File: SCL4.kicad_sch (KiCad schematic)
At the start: 37 parts, among them J2 spare2, J3 Siemens_A1010-A263, J5 SP2, J6 Conn_01x08, J7 5V out, U1 MC3487DX, U2 MC3487DX, U3 TRAM Size 2, U4 MC10H125 (20PLCC), U5 MC10H124 (20PLCC)

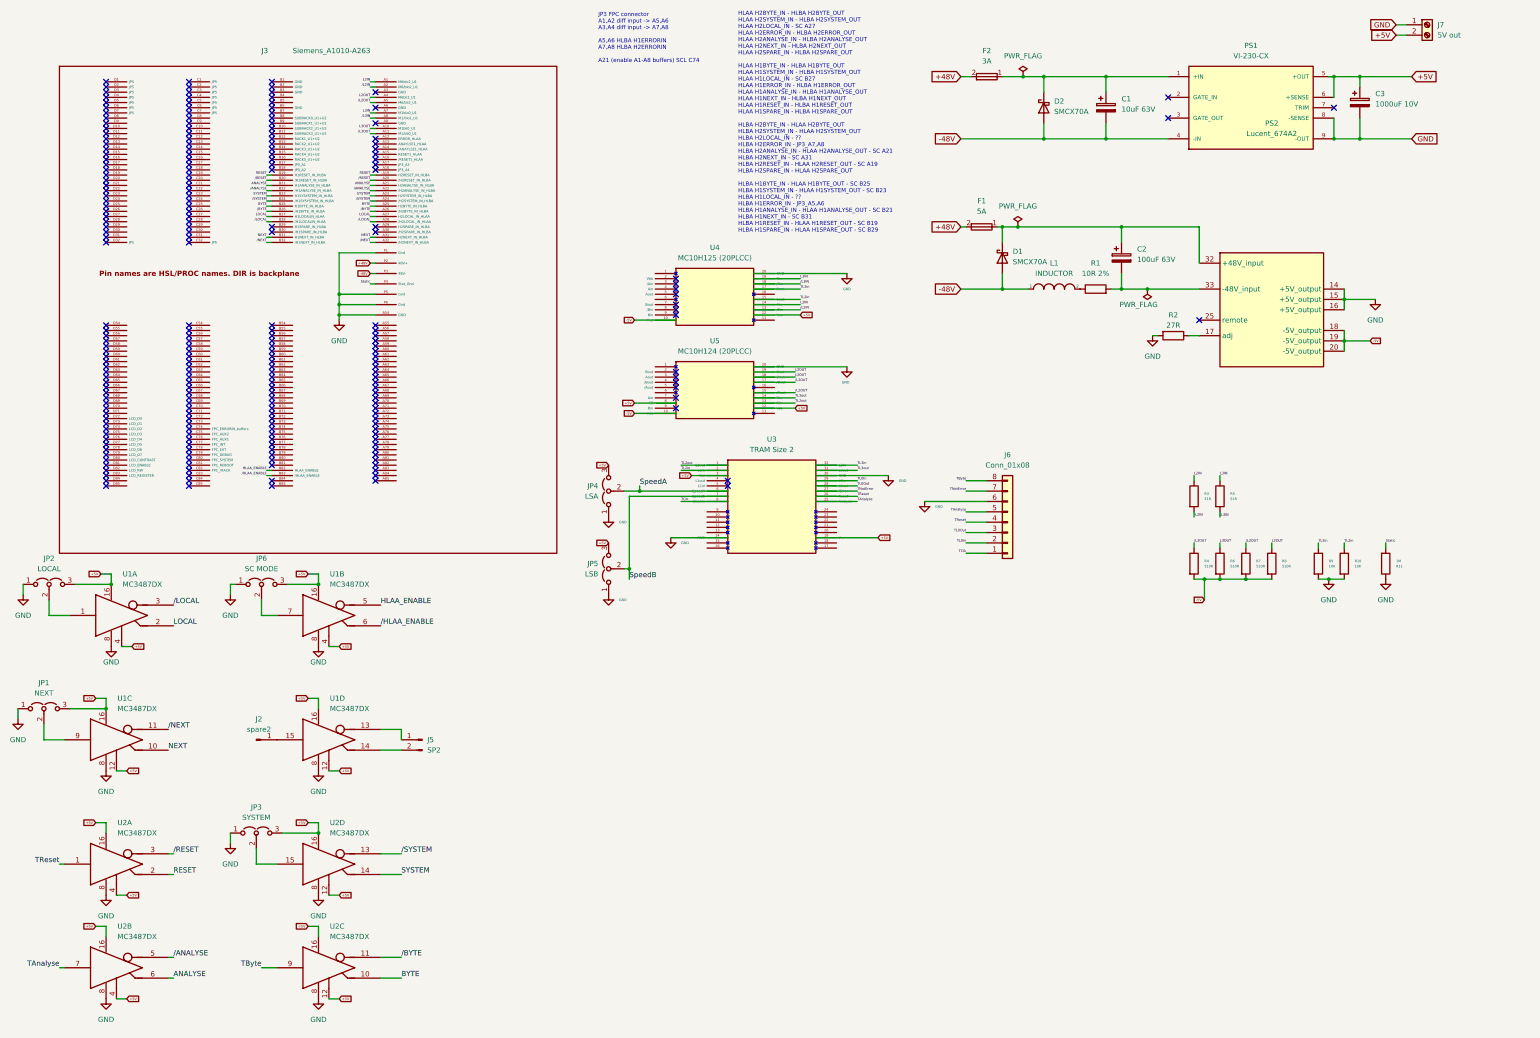
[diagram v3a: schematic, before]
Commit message: Major rework - fix -5V2 PSU orientation - analyse2 & reset2 signals for proc only operation (no HSL) - bring TRAM L1 and L3 to external header - lay down C3 to reduce height - decoupling - reduce + better match ECL trace lengths - remove R1 - reorder J6 to same as rpi interface header
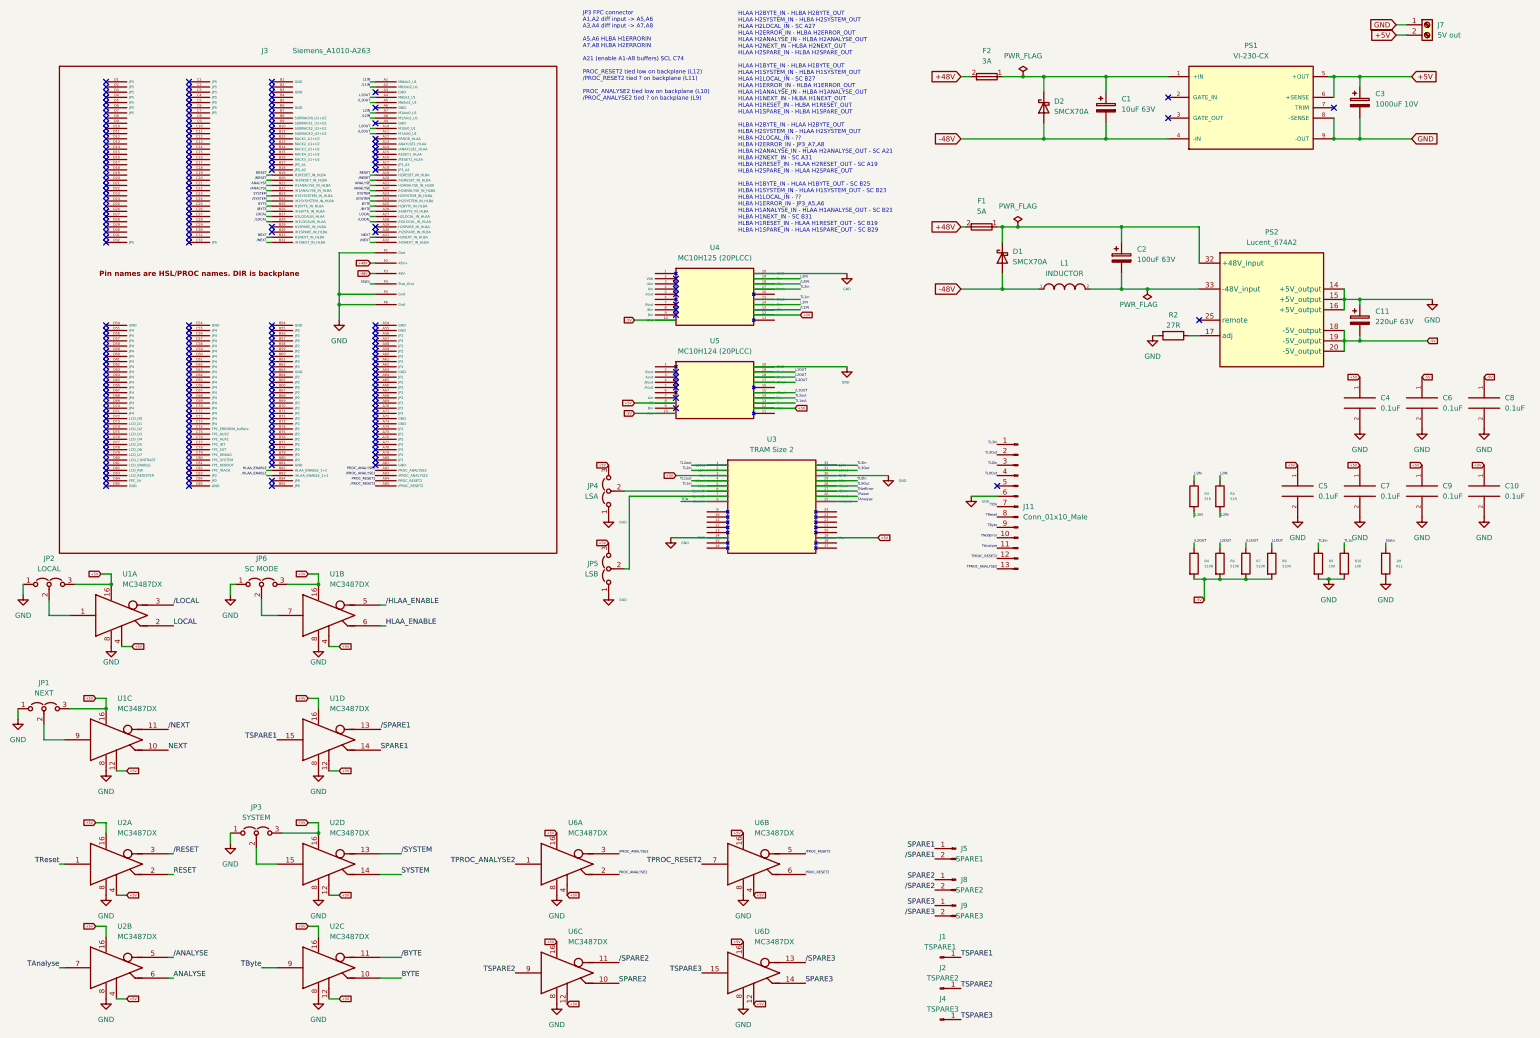
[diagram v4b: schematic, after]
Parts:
- removed J6: Conn_01x08, Connector_PinHeader_2.54mm:PinHeader_1x08_P2.54mm_Vertical, symbol Connector_Generic:Conn_01x08
- removed R1: 10R 2%, Resistor_THT:R_Axial_DIN0207_L6.3mm_D2.5mm_P15.24mm_Horizontal, symbol Device:R
- added C10, C4, C5, C6, C7, C8, C9: 0.1uF, Capacitor_SMD:C_0402_1005Metric_Pad0.74x0.62mm_HandSolder, symbol pspice:C
- added C11: 220uF 63V, Capacitor_THT:C_Radial_D8.0mm_H11.5mm_P3.50mm, symbol Device:C_Polarized
- added J1: TSPARE1, Connector_PinHeader_2.54mm:PinHeader_1x01_P2.54mm_Vertical, symbol Connector:Conn_01x01_Male
- added J11: Conn_01x10_Male, Connector_PinHeader_2.54mm:PinHeader_1x13_P2.54mm_Horizontal, symbol Connector:Conn_01x13_Male
- added J4: TSPARE3, Connector_PinHeader_2.54mm:PinHeader_1x01_P2.54mm_Vertical, symbol Connector:Conn_01x01_Male
- added J8: SPARE2, Connector_PinHeader_2.54mm:PinHeader_1x02_P2.54mm_Vertical, symbol Connector:Conn_01x02_Male
- added J9: SPARE3, Connector_PinHeader_2.54mm:PinHeader_1x02_P2.54mm_Vertical, symbol Connector:Conn_01x02_Male
- added U6: MC3487DX, Package_SO:SOIC-16_3.9x9.9mm_P1.27mm, symbol Interface_LineDriver:MC3487DX
- C3: footprint Capacitor_THT:CP_Radial_D13.0mm_P5.00mm -> Capacitor_THT:C_Radial_D12.5mm_H20.0mm_P5.00mm
- J2: value spare2 -> TSPARE2
- J5: value SP2 -> SPARE1
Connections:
- net L3IN is gone; now on net L2IN: J3.A7 (M1blo0_U1), R5.1, U4.19 (Din)
- net L3OUT is gone; now on net L2OUT: J3.A10 (M1bli0_U1), R6.1, U5.18 (Dout)
- net /L3IN is gone; now on net /L2IN: J3.A8 (M1/blo1_U1), R5.2, U4.18 (/Din)
- net /L3OUT is gone; now on net /L2OUT: J3.A11 (M1/bli0_U1), R4.1, U5.17 (/Dout)
- net +5V: now also C10.1, C4.1, C5.1, C7.1, C9.1, U6.12 (ENABLE), U6.12 (ENABLE), U6.16 (VCC), U6.16 (VCC), U6.16 (VCC), U6.16 (VCC), U6.4 (ENABLE), U6.4 (ENABLE)
- net -5V: now also C11.2, C6.1, C8.1
- net GND: now also C10.2, C11.1, C4.2, C5.2, C6.2, C7.2, C8.2, C9.2, J11.6 (Pin_6), U6.8 (GND), U6.8 (GND), U6.8 (GND), U6.8 (GND); no longer J3.A54 (GND)
- net HLAA_ENABLE: now also U1.6 (OUT+); no longer U1.5 (OUT-)
- net L2IN: no longer J3.A1 (M6blo2_U1), R3.1, U4.14 (Cin)
- net L2OUT: no longer J3.A4 (M6bli2_U1), R8.1, U5.19 (Cout)
- net TAnalyse: now also J11.11 (Pin_11)
- net TByte: now also J11.9 (Pin_9)
- net TClk: now also J11.7 (Pin_7)
- net TL0In: now also J11.3 (Pin_3)
- net TL0Out: now also J11.4 (Pin_4)
- net TL2in: now also R9.1, U4.17 (Dout); no longer R10.1, U4.15 (Cout)
- net TL2out: now also U5.14 (Din); no longer U5.13 (Cin)
- net TNotError: now also J11.10 (Pin_10)
- net TReset: now also J11.8 (Pin_8)
- net /HLAA_ENABLE: now also U1.5 (OUT-); no longer U1.6 (OUT+)
- net /L2IN: no longer J3.A2 (M6/blo2_U1), R3.2, U4.13 (/Cin)
- net /L2OUT: no longer J3.A5 (M6/bli2_U1), R7.1, U5.15 (/Cout)
- net TL1out: now reaches U3.4 (L1out)
- net TL1out: now also U5.13 (Cin)
- net TL1in: now reaches U3.5 (L1in)
- net TL1in: now also R10.1, U4.15 (Cout)
- net SPARE1: now reaches J5.1 (Pin_1)
- net SPARE1: now also U1.14 (OUT+); no longer U1.13 (OUT-)
- net /SPARE1: now reaches J5.2 (Pin_2)
- net /SPARE1: now also U1.13 (OUT-); no longer U1.14 (OUT+)
- net at L1.2: now also C2.2, PS2.33 (-48V_input)
- net TSPARE1: now reaches U1.15 (INPUT)
- net TSPARE1: now also J1.1 (Pin_1); no longer J2.1 (Pin_1)
- net PROC_ANALYSE2: now reaches J3.A82 (PROC_ANALYSE2)
- net PROC_ANALYSE2: now also U6.2 (OUT+)
- net /PROC_ANALYSE2: now reaches J3.A83 (/PROC_ANALYSE2)
- net /PROC_ANALYSE2: now also U6.3 (OUT-)
- net PROC_RESET2: now reaches J3.A84 (PROC_RESET2)
- net PROC_RESET2: now also U6.6 (OUT+)
- net /PROC_RESET2: now reaches J3.A85 (/PROC_RESET2)
- net /PROC_RESET2: now also U6.5 (OUT-)
- net SpeedA: no longer names the net of JP4.2 (C), U3.6 (SpeedA)
- net SpeedB: no longer names the net of JP5.2 (C), U3.7 (SpeedB)
- removed net TL3in: R9.1, U3.32 (L3in), U4.17 (Dout)
- net TL3out renamed TL3Out
- net TL3Out: now also J11.2 (Pin_2); no longer U5.14 (Din)
- new net L1IN: J3.A1 (M6blo2_U1), R3.1, U4.14 (Cin)
- new net L1OUT: J3.A4 (M6bli2_U1), R8.1, U5.19 (Cout)
- new net SPARE2: J8.1 (Pin_1), U6.10 (OUT+)
- new net SPARE3: J9.1 (Pin_1), U6.14 (OUT+)
- new net TL3In: J11.1 (Pin_1), U3.32 (L3in)
- new net TPROC_ANALYSE2: J11.13 (Pin_13), U6.1 (INPUT)
- new net TPROC_RESET2: J11.12 (Pin_12), U6.7 (INPUT)
- new net TSPARE2: J2.1 (Pin_1), U6.9 (INPUT)
- new net TSPARE3: J4.1 (Pin_1), U6.15 (INPUT)
- new net /L1IN: J3.A2 (M6/blo2_U1), R3.2, U4.13 (/Cin)
- new net /L1OUT: J3.A5 (M6/bli2_U1), R7.1, U5.15 (/Cout)
- new net /SPARE2: J8.2 (Pin_2), U6.11 (OUT-)
- new net /SPARE3: J9.2 (Pin_2), U6.13 (OUT-)
- no-connect marks 240 -> 236
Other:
- note added: "JP3 FPC connector A1,A2 diff input -> A5,A6 A3,A4 diff input -> A7,A8 A5,A6 HLBA H1ERRORIN A7,A8 HLBA H2ERRORIN A21 (enable A1-A8 buffers) SCL C74 PROC_RESET2 tied low on backplane (L12) /PROC_RESET2 tied ? on backplane (L11) PROC_ANALYSE2 tied low on backplane (L10) /PROC_ANALYSE2 tied ? on backplane (L9)"
- note removed: "JP3 FPC connector A1,A2 diff input -> A5,A6 A3,A4 diff input -> A7,A8 A5,A6 HLBA H1ERRORIN A7,A8 HLBA H2ERRORIN A21 (enable A1-A8 buffers) SCL C74"
- moved on the sheet: L1

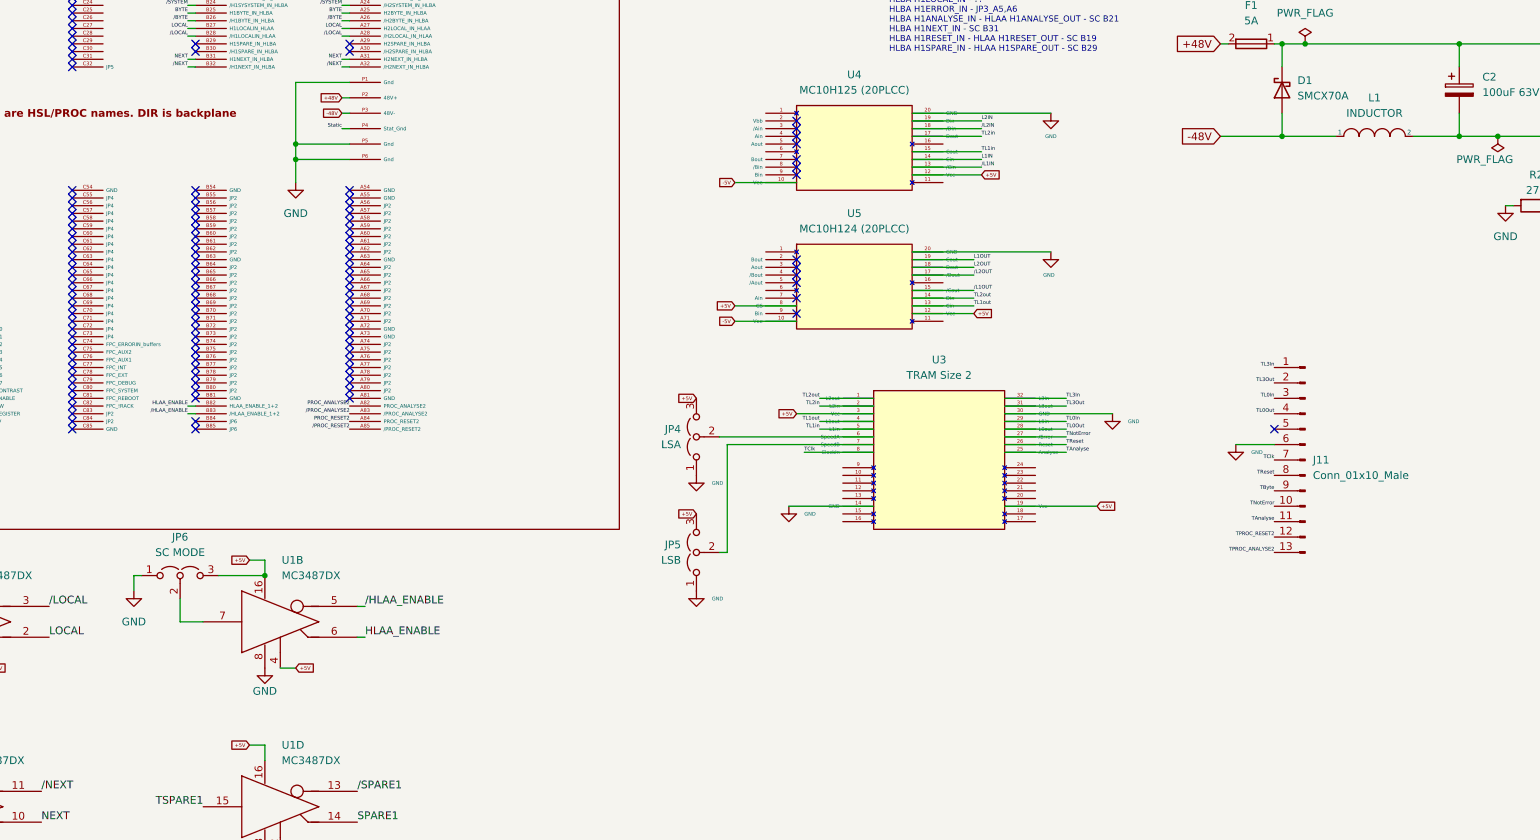
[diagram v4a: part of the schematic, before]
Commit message: Use RJ45 external and add thermal pads
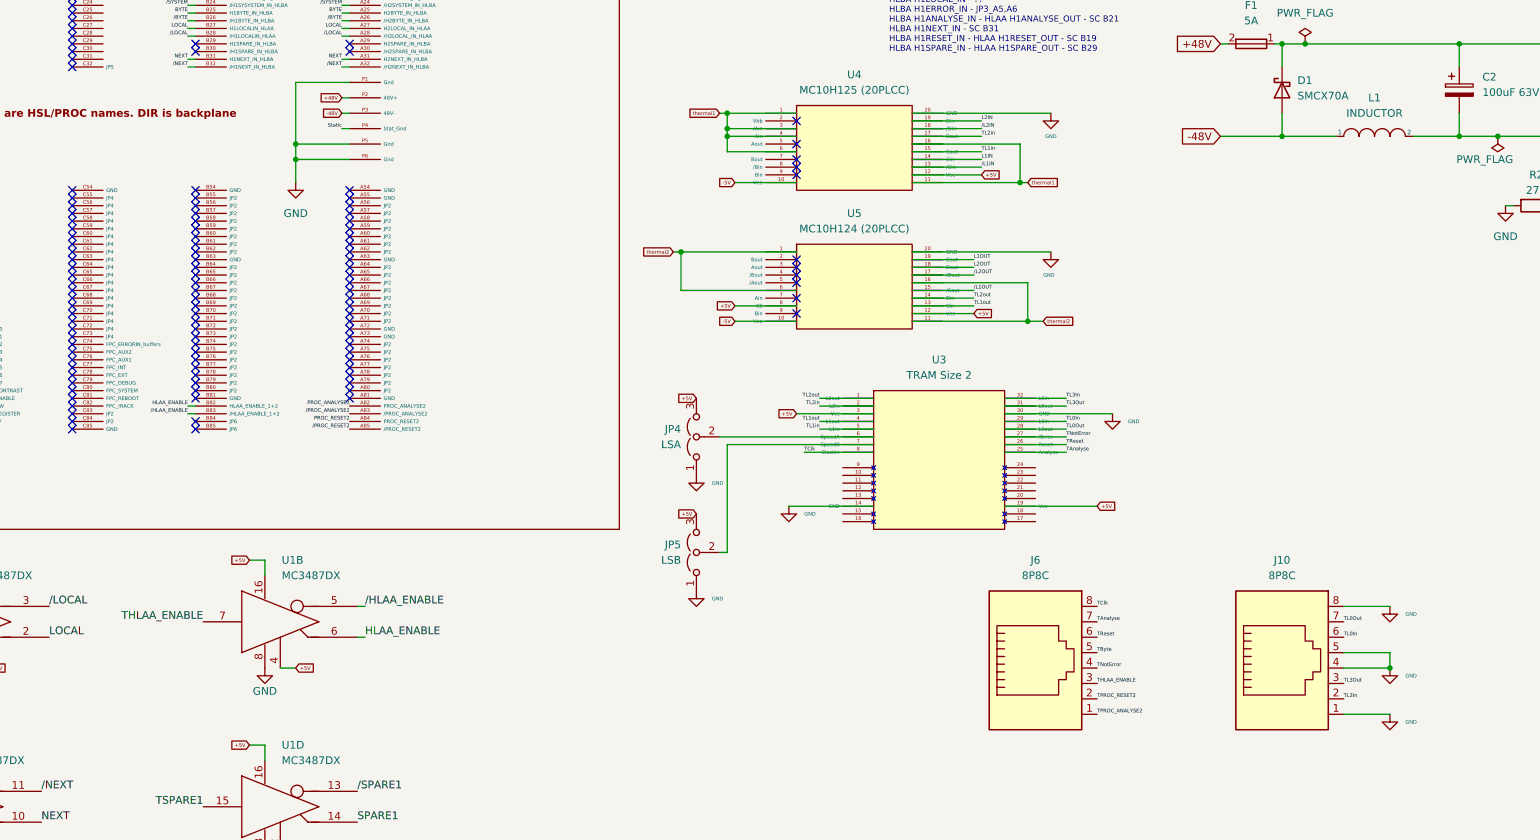
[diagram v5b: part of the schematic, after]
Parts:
- removed J11: Conn_01x10_Male, Connector_PinHeader_2.54mm:PinHeader_1x13_P2.54mm_Horizontal, symbol Connector:Conn_01x13_Male
- removed JP6: SC MODE, Connector_PinHeader_2.54mm:PinHeader_1x03_P2.54mm_Vertical, symbol Jumper:Jumper_3_Open
- added J10, J6: 8P8C, Connector_RJ:RJ45_Ninigi_GE, symbol Connector:8P8C
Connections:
- net GND: now also J10.1, J10.4, J10.5, J10.8
- net TAnalyse: now also J6.7
- net TByte: now also J6.5
- net TClk: now also J6.8
- net TL0In: now also J10.6
- net TL0Out: now also J10.7
- net TL3In: now also J10.2
- net TL3Out: now also J10.3
- net TNotError: now also J6.4
- net TPROC_ANALYSE2: now also J6.1
- net TPROC_RESET2: now also J6.2
- net TReset: now also J6.6
- net thermal1: now reaches U4.1
- net thermal1: now also U4.11, U4.16, U4.3 (/Ain), U4.4 (Ain), U4.6
- net THLAA_ENABLE: now reaches U1.7 (INPUT)
- net THLAA_ENABLE: now also J6.3
- net thermal2: now reaches U5.1
- net thermal2: now also U5.11, U5.16, U5.6
- no-connect marks 236 -> 233

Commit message: more LEDs
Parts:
- added D3: 5V OK, LED_THT:LED_Rectangular_W5.0mm_H2.0mm, symbol Device:LED
- added D4: -5V OK, LED_THT:LED_Rectangular_W5.0mm_H2.0mm, symbol Device:LED
- added D5: Reset, LED_THT:LED_Rectangular_W5.0mm_H2.0mm, symbol Device:LED
- added D6: Error, LED_THT:LED_Rectangular_W5.0mm_H2.0mm, symbol Device:LED
- added R1, R12, R13, R14: 220R, Resistor_SMD:R_1206_3216Metric_Pad1.30x1.75mm_HandSolder, symbol Device:R
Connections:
- net +5V: now also R1.2, R14.2
- net -5V: now also D4.1 (K)
- net GND: now also D3.1 (K), D5.1 (K), R12.2
- net TNotError: now also D6.1 (K)
- net TReset: now also R13.2
- new net: D3.2 (A), R1.1
- new net: D6.2 (A), R14.1
- new net: D5.2 (A), R13.1
- new net: D4.2 (A), R12.1
